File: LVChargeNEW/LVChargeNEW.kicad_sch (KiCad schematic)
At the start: 45 parts, among them Q1 CSD15380F3T, Q2 CSD15380F3T, Q3 CSD15380F3T, Q4 CSD15380F3T, U1 PQ25856QWRRVRQ1

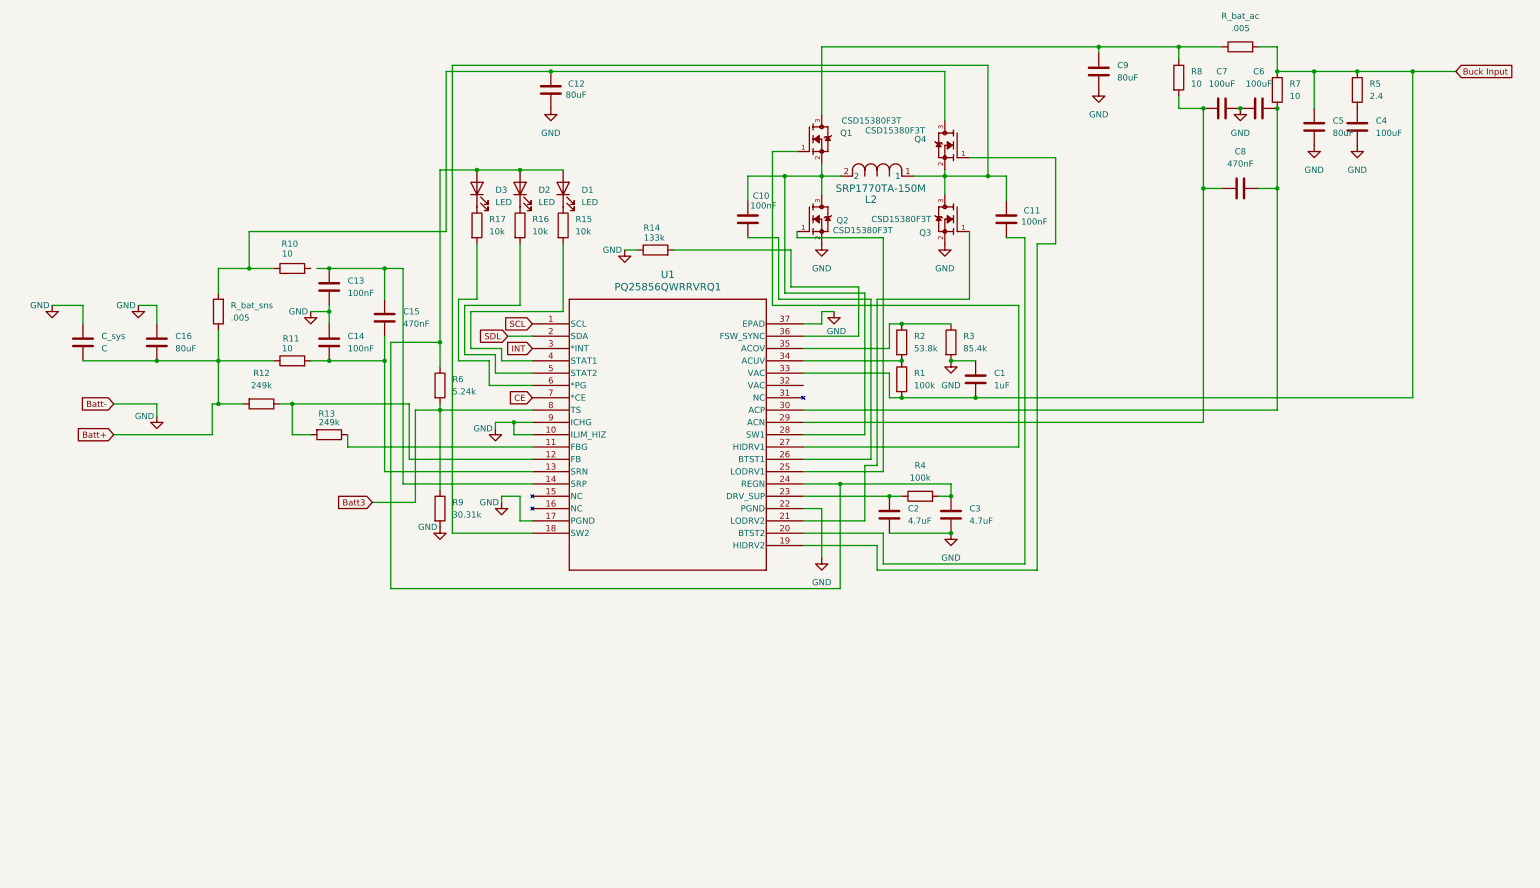
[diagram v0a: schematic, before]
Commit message: Added LED, C and R footprints
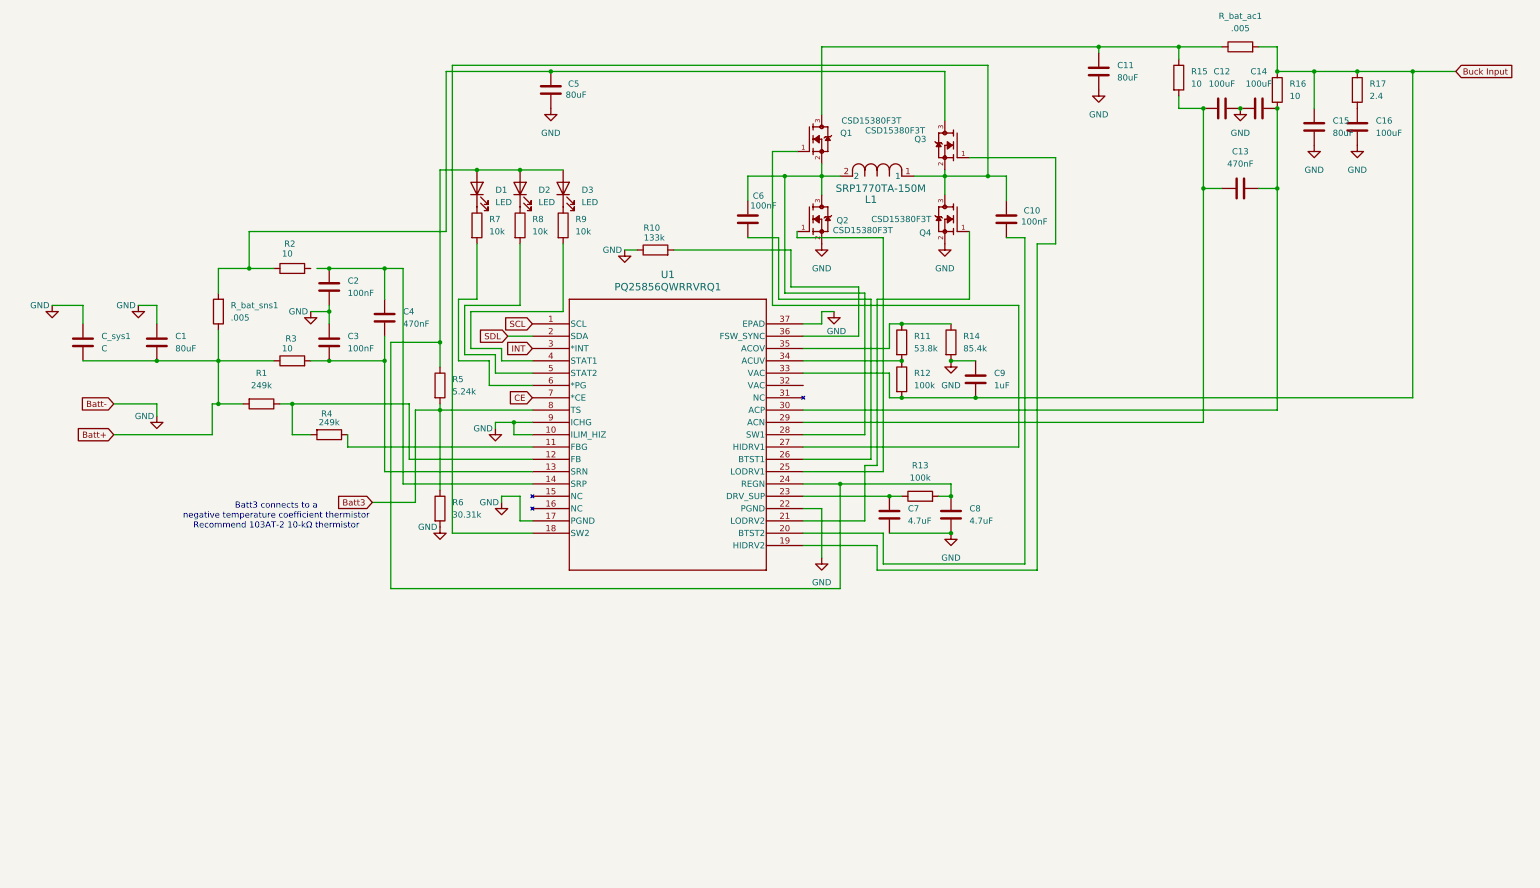
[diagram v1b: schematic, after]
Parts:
- C1: renamed from C16; footprint (none) -> Capacitor_THT:C_Radial_D5.0mm_H11.0mm_P2.00mm
- C10: renamed from C11; footprint (none) -> Capacitor_THT:C_Radial_D5.0mm_H11.0mm_P2.00mm
- C11: renamed from C9; footprint (none) -> Capacitor_THT:C_Radial_D5.0mm_H11.0mm_P2.00mm
- C12: renamed from C7; footprint (none) -> Capacitor_THT:C_Radial_D5.0mm_H11.0mm_P2.00mm
- C13: renamed from C8; footprint (none) -> Capacitor_THT:C_Radial_D5.0mm_H11.0mm_P2.00mm
- C14: renamed from C6; footprint (none) -> Capacitor_THT:C_Radial_D5.0mm_H11.0mm_P2.00mm
- C15: renamed from C5; footprint (none) -> Capacitor_THT:C_Radial_D5.0mm_H11.0mm_P2.00mm
- C16: renamed from C4; footprint (none) -> Capacitor_THT:C_Radial_D5.0mm_H11.0mm_P2.00mm
- C2: renamed from C13; footprint (none) -> Capacitor_THT:C_Radial_D5.0mm_H11.0mm_P2.00mm
- C3: renamed from C14; footprint (none) -> Capacitor_THT:C_Radial_D5.0mm_H11.0mm_P2.00mm
- C4: renamed from C15; footprint (none) -> Capacitor_THT:C_Radial_D5.0mm_H11.0mm_P2.00mm
- C5: renamed from C12; footprint (none) -> Capacitor_THT:C_Radial_D5.0mm_H11.0mm_P2.00mm
- C6: renamed from C10; footprint (none) -> Capacitor_THT:C_Radial_D5.0mm_H11.0mm_P2.00mm
- C7: renamed from C2; footprint (none) -> Capacitor_THT:C_Radial_D5.0mm_H11.0mm_P2.00mm
- C8: renamed from C3; footprint (none) -> Capacitor_THT:C_Radial_D5.0mm_H11.0mm_P2.00mm
- C9: renamed from C1; footprint (none) -> Capacitor_THT:C_Radial_D5.0mm_H11.0mm_P2.00mm
- D1: renamed from D3; footprint (none) -> LED_SMD:LED_1206_3216Metric
- D2: footprint (none) -> LED_SMD:LED_1206_3216Metric
- D3: renamed from D1; footprint (none) -> LED_SMD:LED_1206_3216Metric
- R1: renamed from R12; footprint (none) -> Resistor_THT:R_Axial_DIN0207_L6.3mm_D2.5mm_P7.62mm_Horizontal
- R10: renamed from R14; footprint (none) -> Resistor_THT:R_Axial_DIN0207_L6.3mm_D2.5mm_P7.62mm_Horizontal
- R11: renamed from R2; footprint (none) -> Resistor_THT:R_Axial_DIN0207_L6.3mm_D2.5mm_P7.62mm_Horizontal
- R12: renamed from R1; footprint (none) -> Resistor_THT:R_Axial_DIN0207_L6.3mm_D2.5mm_P7.62mm_Horizontal
- R13: renamed from R4; footprint (none) -> Resistor_THT:R_Axial_DIN0207_L6.3mm_D2.5mm_P7.62mm_Horizontal
- R14: renamed from R3; footprint (none) -> Resistor_THT:R_Axial_DIN0207_L6.3mm_D2.5mm_P7.62mm_Horizontal
- R15: renamed from R8; footprint (none) -> Resistor_THT:R_Axial_DIN0207_L6.3mm_D2.5mm_P7.62mm_Horizontal
- R16: renamed from R7; footprint (none) -> Resistor_THT:R_Axial_DIN0207_L6.3mm_D2.5mm_P7.62mm_Horizontal
- R17: renamed from R5; footprint (none) -> Resistor_THT:R_Axial_DIN0207_L6.3mm_D2.5mm_P7.62mm_Horizontal
- R2: renamed from R10; footprint (none) -> Resistor_THT:R_Axial_DIN0207_L6.3mm_D2.5mm_P7.62mm_Horizontal
- R3: renamed from R11; footprint (none) -> Resistor_THT:R_Axial_DIN0207_L6.3mm_D2.5mm_P7.62mm_Horizontal
- R4: renamed from R13; footprint (none) -> Resistor_THT:R_Axial_DIN0207_L6.3mm_D2.5mm_P7.62mm_Horizontal
- R5: renamed from R6; footprint (none) -> Resistor_THT:R_Axial_DIN0207_L6.3mm_D2.5mm_P7.62mm_Horizontal
- R6: renamed from R9; footprint (none) -> Resistor_THT:R_Axial_DIN0207_L6.3mm_D2.5mm_P7.62mm_Horizontal
- R7: renamed from R17; footprint (none) -> Resistor_THT:R_Axial_DIN0207_L6.3mm_D2.5mm_P7.62mm_Horizontal
- R8: renamed from R16; footprint (none) -> Resistor_THT:R_Axial_DIN0207_L6.3mm_D2.5mm_P7.62mm_Horizontal
- R9: renamed from R15; footprint (none) -> Resistor_THT:R_Axial_DIN0207_L6.3mm_D2.5mm_P7.62mm_Horizontal
- renumbered C_sys to C_sys1, L2 to L1, Q4 to Q3, Q3 to Q4, R_bat_ac to R_bat_ac1, R_bat_sns to R_bat_sns1
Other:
- note added: "Batt3 connects to a negative temperature coefficient thermistor Recommend 103AT-2 10-kΩ thermistor"

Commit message: Updated GLVCharge Schematic
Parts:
- removed Q1, Q2, Q3, Q4: CSD15380F3T, CSD15380F3T:TRXDFN69X60X35-3N, symbol LVChargeNEWLocalLib:CSD15380F3T
- added MOSFET1, MOSFET2, MOSFET3, MOSFET4: IPZ40N04S5L7R4ATMA1, mosfet:PG-TSDSON-8-32_INF, symbol 2025-10-30_20-54-56:IPZ40N04S5L7R4ATMA1
- L1: value SRP1770TA-150M -> 10u; footprint IND_SRP1770_BRN -> mosfet:inductor
- U1: footprint VQFN36_RRV_TEX -> chip:VQFN36_RRV_TEX
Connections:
- net GND: now also MOSFET2.1, MOSFET2.2, MOSFET2.3, MOSFET4.1, MOSFET4.2, MOSFET4.3
- net at U1.19 (HIDRV2): now also MOSFET3.4
- net at C10.2, L1.1, U1.18 (SW2): now also MOSFET3.1, MOSFET3.2, MOSFET3.3, MOSFET4.5, MOSFET4.6, MOSFET4.7, MOSFET4.8
- net at C5.2, R2.1, R_bat_sns1.2: now also MOSFET3.5, MOSFET3.6, MOSFET3.7, MOSFET3.8
- net at C6.2, L1.2, U1.28 (SW1): now also U1.27 (HIDRV1), MOSFET1.1, MOSFET1.2, MOSFET1.3, MOSFET1.4, MOSFET2.5, MOSFET2.6, MOSFET2.7, MOSFET2.8
- net at C11.2, R15.1, R_bat_ac1.1: now also MOSFET1.5, MOSFET1.6, MOSFET1.7, MOSFET1.8
- net at U1.25 (LODRV1): now also MOSFET2.4
- net at U1.21 (LODRV2): now also MOSFET4.4
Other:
- moved on the sheet: C1, C10, C11, C12, C13, C14, C15, C16, C2, C3, C4, C5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

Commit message: Uploaded Sean's stuff
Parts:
- removed MOSFET1, MOSFET2, MOSFET3, MOSFET4: IPZ40N04S5L7R4ATMA1, mosfet:PG-TSDSON-8-32_INF, symbol 2025-10-30_20-54-56:IPZ40N04S5L7R4ATMA1
- added Q1, Q2, Q3, Q4: CSD15380F3T, CSD15380F3T:TRXDFN69X60X35-3N, symbol LVChargeNEWLocalLib:CSD15380F3T
- L1: value 10u -> SRP1770TA-150M; footprint mosfet:inductor -> IND_SRP1770_BRN
- U1: footprint chip:VQFN36_RRV_TEX -> VQFN36_RRV_TEX
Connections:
- net GND: now also Q2.2, Q4.2
- net at U1.21 (LODRV2): now also Q4.1
- net at C10.2, L1.1, U1.18 (SW2): now also Q3.2, Q4.3
- net at C6.2, L1.2, U1.28 (SW1): now also Q1.2, Q2.3; no longer U1.27 (HIDRV1)
- net at C11.2, R15.1, R_bat_ac1.1: now also Q1.3
- net at U1.25 (LODRV1): now also Q2.1
- net at U1.19 (HIDRV2): now also Q3.1
- net at C5.2, R2.1, R_bat_sns1.2: now also Q3.3
- new net: Q1.1, U1.27 (HIDRV1)
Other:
- moved on the sheet: C1, C10, C11, C12, C13, C14, C15, C16, C2, C3, C4, C5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
